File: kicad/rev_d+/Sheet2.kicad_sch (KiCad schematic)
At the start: 199 parts, among them J10 vg_old, J12 JUMPER, J13 RJ45_Hanrun_HR911105A_Horizon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, J5 JUMPER, J6 JUMPER, J8 JUMPER, J9 JUMPER, Q2 QUARTZ, Q3 QUARTZ32768, X11 KEYB-MOUSE, X12 IDC20, X13 USB_C, X15 PLB2-2, X19 WCH LinkE pgm conn, X21 Turbosound conn, X22 PS2 extra input, X23 SEGA pads, X25 USB_C device, X27 USB_A, X3 IDC26LPT, X4 IDC10M, X5 IDC10M, X6 RS232_9

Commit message: pentevo: rev D+: PS/2 WIP
git-svn-id: svn://localhost/local-pentevo@1303 c6c76956-fad2-4150-a3a9-ea0a427205ba
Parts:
- added C65: 10uF, EC-CHIP, symbol eva-altium-import:Sheet1_0_ECAPCHIP
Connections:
- net GND: now also C65.2
- net VCC33_MCU: no longer L6.1
- net VCC3V3: now also R32.1 (i/o), R33.1 (i/o), R34.1 (i/o)
- net VCC5: no longer R32.1 (i/o), R33.1 (i/o), R34.1 (i/o)
- net VCC5_MCU: now also L6.1; no longer X27.1 (VBUS)
- net at C59.1, XSD2.4 (VDD): no longer L6.2
- new net: C65.1, L6.2, X27.1 (VBUS)
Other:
- moved on the sheet: R32, R33, R34, R60, R61, R62, X19

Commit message: pentevo: rev D+: PS/2 WIP
git-svn-id: svn://localhost/local-pentevo@1304 c6c76956-fad2-4150-a3a9-ea0a427205ba
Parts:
- added L7: 1uH, L-CHIP, symbol eva-altium-import:Sheet1_1_L-CHIP
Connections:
- net VCC33_MCU: now also L7.1
- net at C59.1, XSD2.4 (VDD): now also L7.2
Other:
- moved on the sheet: C38, C39, C4, C5, C7, C8, J12, J5, J9, Q2, Q3, R153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

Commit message: pentevo: rev D+: PS/2 WIP
git-svn-id: svn://localhost/local-pentevo@1305 c6c76956-fad2-4150-a3a9-ea0a427205ba
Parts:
- removed R200: 5K1, R-CHIP, symbol eva-altium-import:Sheet2_0_mirrored_RESCHIP
- added R200: 10K, R-CHIP, symbol eva-altium-import:Sheet1_1_RESCHIP
- added R203: 24k, R-CHIP, symbol eva-altium-import:Sheet2_3_RESCHIP
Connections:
- net ATX_POWERON: now also R25.1 (i/o)
- net GND: now also R203.1 (i/o)
- net PS2_KB_CLK_I: now also D4.98 (PE1)
- net PS2_KB_CLK_O: now also D4.24 (PA1)
- net PS2_KB_DAT_I: now also D4.97 (PE0)
- net PS2_KB_DAT_O: now also D4.23 (PA0)
- net PS2_MS_CLK_I: now also D4.2 (PE3)
- net PS2_MS_CLK_O: now also D4.26 (PA3)
- net PS2_MS_DAT_I: now also D4.1 (PE2)
- net PS2_MS_DAT_O: now also D4.25 (PA2)
- net USBDEV_VBUS: now reaches D4.68 (PA9/OTG_VBUS)
- net USBDEV_VBUS: now also R200.2 (i/o1), R203.2 (i/o1)
- net at X25.A4 (VBUS), X25.A9 (VBUS), X25.B4 (VBUS)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: now also R200.1 (i/o)
- no-connect marks 39 -> 38
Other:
- moved on the sheet: R25, R35, VD6

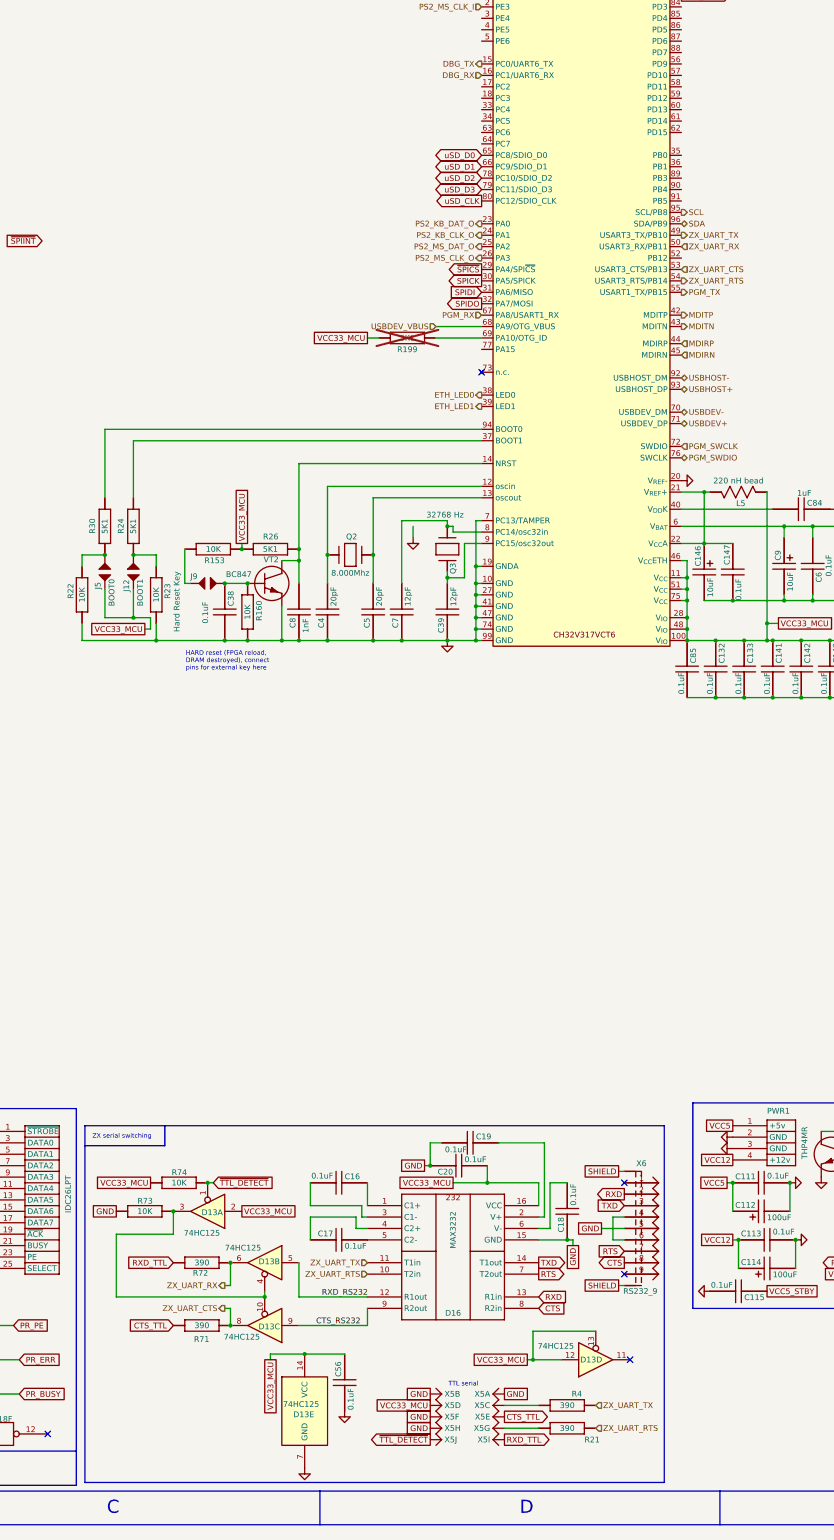
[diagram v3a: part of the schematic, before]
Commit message: pentevo: rev D+: PS/2 done, separate UARTs per TTL and RS232
git-svn-id: svn://localhost/local-pentevo@1306 c6c76956-fad2-4150-a3a9-ea0a427205ba
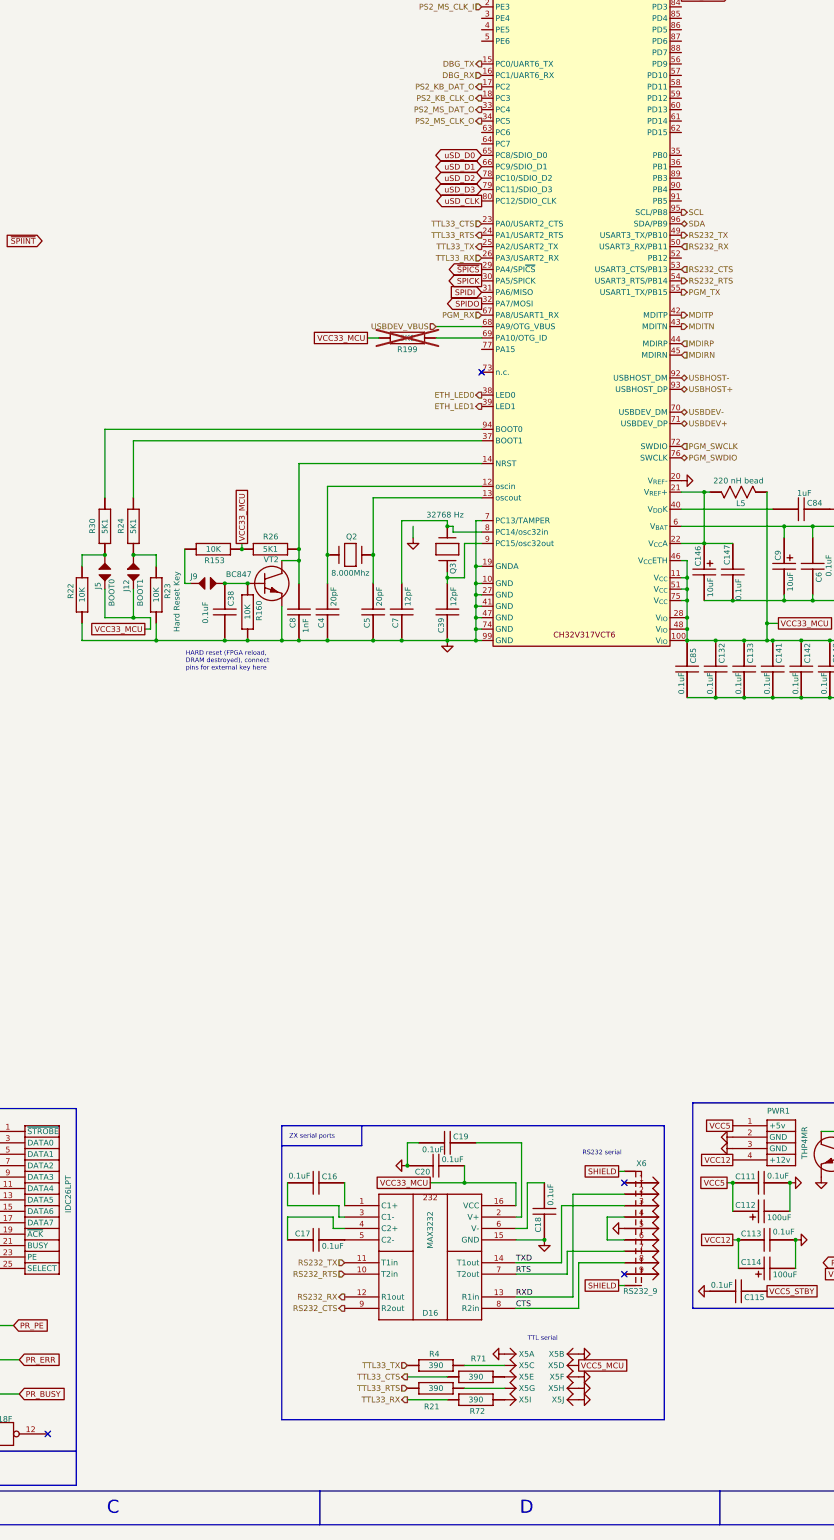
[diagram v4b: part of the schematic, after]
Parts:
- removed C56: 0.1uF, C-CHIP, symbol eva-altium-import:Sheet2_3_mirrored_CAPCHIP
- removed D13: 74HC125, symbol 74xx:74LS125
- removed R73, R74: 10K, R-CHIP, symbol eva-altium-import:Sheet2_2_RESCHIP
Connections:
- net ~{TTL_DETECT} is gone; now on net GND: X5.10
- net PS2_KB_CLK_O: now also D4.18 (PC3); no longer D4.24 (PA1)
- net PS2_KB_DAT_O: now also D4.17 (PC2); no longer D4.23 (PA0)
- net PS2_MS_CLK_O: now also D4.34 (PC5); no longer D4.26 (PA3)
- net PS2_MS_DAT_O: now also D4.33 (PC4); no longer D4.25 (PA2)
- net VCC33_MCU: no longer X5.4
- net VCC5_MCU: now also X5.4
- net CTS_RS232 renamed RS232_CTS
- net RS232_CTS: now also D4.53 (USART3_CTS/PB13)
- net CTS_TTL: no longer names the net of R71.1 (i/o), X5.5
- net RXD_RS232 renamed RS232_RX
- net RS232_RX: now also D4.50 (USART3_RX/PB11)
- net RXD_TTL: no longer names the net of R72.1 (i/o), X5.9
- net ZX_UART_CTS renamed TTL33_CTS
- net TTL33_CTS: now also D4.23 (PA0/USART2_CTS); no longer D4.53 (USART3_CTS/PB13)
- net ZX_UART_RTS renamed RS232_RTS
- net RS232_RTS: no longer R21.2 (i/o1)
- net ZX_UART_RX renamed TTL33_RX
- net TTL33_RX: now also D4.26 (PA3/USART2_RX); no longer D4.50 (USART3_RX/PB11)
- net ZX_UART_TX renamed RS232_TX
- net RS232_TX: no longer R4.1 (i/o)
- new net TTL33_RTS: D4.24 (PA1/USART2_RTS), R21.2 (i/o1)
- new net TTL33_TX: D4.25 (PA2/USART2_TX), R4.1 (i/o)
- no-connect marks 38 -> 37
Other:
- note added: "ZX serial ports"
- note removed: "ZX serial switching"
- moved on the sheet: C16, C17, C18, C19, C20, D16, R21, R4, R71, R72, X5A, X5B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

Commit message: pentevo: rev D+: zx kbd
git-svn-id: svn://localhost/local-pentevo@1307 c6c76956-fad2-4150-a3a9-ea0a427205ba
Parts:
- removed R152, R161: 1K, R-CHIP, symbol eva-altium-import:Sheet2_3_RESCHIP
- removed VT3: BC847, Package_TO_SOT_SMD:SOT-23_Handsoldering, symbol eva-altium-import:Sheet2_0_mirrored_BC847
- added C56: 20pF, C-CHIP, symbol eva-altium-import:Sheet2_0_CAPCHIP
- added J13, J14: JUMPER, JUMPER, symbol eva-altium-import:Sheet2_3_JUMPER
- added R152, R161: 5K1, R-CHIP, symbol eva-altium-import:Sheet2_0_RESCHIP
- added R19, R205: 390, R-CHIP, symbol eva-altium-import:Sheet1_0_RESCHIP
- added R204: 5K1, R-CHIP, symbol eva-altium-import:Sheet2_1_RESCHIP
- added R206: 470K, Resistor_SMD:R_0805_2012Metric_Pad1.20x1.40mm_HandSolder, symbol Device:R
- added R73: 1K, Resistor_SMD:R_0805_2012Metric_Pad1.20x1.40mm_HandSolder, symbol Device:R
- added R74: 390, R-CHIP, symbol eva-altium-import:Sheet2_0_RESCHIP
- added VD3: LED, LED_SMD:LED_0805_2012Metric_Pad1.15x1.40mm_HandSolder, symbol eva-altium-import:Sheet1_0_mirrored_LED
- added VT3, VT4: BC847, Package_TO_SOT_SMD:SOT-23_Handsoldering, symbol Transistor_BJT:BC847
- R36, R37, R38, R39, R40, R41, R42, R43, R44, R45: value 10K -> 5K1
- VD6: footprint LED100 -> LED_SMD:LED_0805_2012Metric_Pad1.15x1.40mm_HandSolder
- renumbered J13 to X28
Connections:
- net ATX_POWERON: now also R73.1, VT3.1 (B)
- net GND: now also R36.1 (i/o), R37.1 (i/o), R38.1 (i/o), R39.1 (i/o), R40.1 (i/o), R73.2, VT3.2 (E), VT4.2 (E)
- net JOYD: now also D4.81 (PD0)
- net JOYF: now also D4.85 (PD4)
- net JOYL: now also D4.82 (PD1)
- net JOYR: now also D4.84 (PD3)
- net JOYU: now also D4.86 (PD5)
- net NMIKEY: now also D4.5 (PE6), R152.2 (i/o1)
- net TAPE_BIT: now also D4.64 (PC7), C56.2, R206.1; no longer D20.8
- net VCC33_MCU: now also R41.1 (i/o), R42.1 (i/o), R43.1 (i/o), R44.1 (i/o), R45.1 (i/o), R152.1 (i/o), R161.1 (i/o); no longer VD6.A
- net VCC5: now also R19.1 (i/o), R205.1 (i/o)
- net VCC5_MCU: now also VD6.A, J13.0 (1); no longer R36.1 (i/o), R37.1 (i/o), R38.1 (i/o), R39.1 (i/o), R40.1 (i/o), R41.1 (i/o), R42.1 (i/o), R43.1 (i/o), R44.1 (i/o), R45.1 (i/o)
- net ZXCOL0: now also D4.35 (PB0)
- net ZXCOL1: now also D4.36 (PB1)
- net ZXCOL2: now also D4.89 (PB3)
- net ZXCOL3: now also D4.90 (PB4)
- net ZXCOL4: now also D4.91 (PB5)
- net ZXROW0: now also D4.88 (PD7)
- net ZXROW1: now also D4.56 (PD9)
- net ZXROW2: now also D4.57 (PD10)
- net ZXROW3: now also D4.58 (PD11)
- net ZXROW4: now also D4.59 (PD12)
- net ZXROW5: now also D4.60 (PD13)
- net ZXROW6: now also D4.61 (PD14)
- net ZXROW7: now also D4.62 (PD15)
- net ~{SOFTRST}: now also D4.4 (PE5), R161.2 (i/o1)
- net ~{SPIINT}: now also D4.3 (PE4)
- net at R25.2 (i/o1): now also D4.77 (PA15)
- net at PWR2.14 (~{PS_ON}): now also VT3.3 (C)
- net ~{PWR_LED}: now reaches R35.1 (i/o)
- net ~{PWR_LED}: now also R74.1 (i/o), VT4.3 (C)
- net at D4.63 (PC6): now also R204.2 (i/o1)
- new net: J13.1 (2), R74.2 (i/o1)
- new net: J14.1 (2), R205.2 (i/o1)
- new net: C56.1, D20.8, R206.2
- new net: R19.2 (i/o1), VD3.A
- new net: R204.1 (i/o), VT4.1 (B)
- new net ~{DISK_LED}: J14.0 (1), VD3.K
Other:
- moved on the sheet: C16, C17, C18, C19, C20, C37, D16, D20D, D20E, D20F, J6, J8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

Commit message: pentevo: rev D+: return back shared UART between TTL and RS232, connect ROM high addrs to MCU
git-svn-id: svn://localhost/local-pentevo@1309 c6c76956-fad2-4150-a3a9-ea0a427205ba
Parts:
- removed C16: 0.1uF, C-CHIP, symbol eva-altium-import:Sheet2_0_mirrored_CAPCHIP
- removed C17: 0.1uF, C-CHIP, symbol eva-altium-import:Sheet2_0_CAPCHIP
- removed C18: 0.1uF, C-CHIP, symbol eva-altium-import:Sheet2_1_CAPCHIP
- removed R21, R4: 390, R-CHIP, symbol eva-altium-import:Sheet2_0_mirrored_RESCHIP
- removed unit 9 of X5
- removed unit 5 of X5
- removed unit 7 of X5
- removed unit 1 of X5
- removed unit 3 of X5
- removed X6: RS232_9, DSUB-9, symbol eva-altium-import:Sheet2_0_mirrored_RS232_9
- added C16: 0.1uF, C-CHIP, symbol eva-altium-import:Sheet2_0_CAPCHIP
- added C17: 0.1uF, C-CHIP, symbol eva-altium-import:Sheet2_3_mirrored_CAPCHIP
- added C18: 0.1uF, C-CHIP, symbol eva-altium-import:Sheet2_0_mirrored_CAPCHIP
- added C82: 0.1uF, C-CHIP, symbol eva-altium-import:Sheet2_1_CAPCHIP
- added D13: 74HC125, symbol 74xx:74LS125
- added R207, R208: 390, R-CHIP, symbol eva-altium-import:Sheet2_0_mirrored_RESCHIP
- added R21, R4: 10K, R-CHIP, symbol eva-altium-import:Sheet2_2_RESCHIP
- added X29: RS232_9, DSUB-9, symbol eva-altium-import:Sheet2_0_mirrored_RS232_9
- added X6: IDC10M, IDC10M, symbol eva-altium-import:Sheet2_2_IDC10M
- R151: value 1K -> 47K
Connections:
- net CTS is gone; now on net RS232_CTS: D16.8 (R2in)
- net RTS is gone; now on net RS232_RTS: D16.7 (T2out)
- net GND: now also C19.1, C20.2, C17.2, C82.1, D13.7 (GND), R4.1 (i/o), X29.5, X6.1; no longer C19.2, C20.1, X5.10
- net PLLS0: now also D4.26 (PA3)
- net PLLS1: now also D4.52 (PB12)
- net PWRGOOD: now also R151.2 (i/o1); no longer R151.1 (i/o)
- net RS232_CTS: now also X29.8; no longer D16.9 (R2out), D4.53 (USART3_CTS/PB13)
- net RS232_RTS: now also X29.7; no longer D16.10 (T2in), D4.54 (USART3_RTS/PB14)
- net SHIELD: now also X29.10, X29.11
- net VCC33_MCU: now also C19.2, C17.1, D13.12, D13.13, D13.14 (VCC), D13.2, R21.2 (i/o1); no longer C20.2
- net at R72.1 (i/o): now also X6.5
- net at D16.2 (V+): now also C20.1; no longer C19.1
- net at R71.1 (i/o): now also X6.9
- net at D30.19 (IO1_6): no longer VT7.3 (D)
- net at D30.18 (IO1_5): no longer VT8.3 (D)
- net at D30.20 (IO1_7): no longer VT6.3 (D)
- net at D16.6 (V-): now also C82.2
- net at D16.1 (C1+): now also C18.1
- net at D16.3 (C1-): now also C18.2
- net at D16.4 (C2+): now also C16.1
- net at D16.5 (C2-): now also C16.2
- net at D4.87 (PD6): now also R151.1 (i/o)
- net RS232_RX: no longer names the net of D16.12 (R1out)
- net RS232_RX: now also D13.5; no longer D4.50 (USART3_RX/PB11)
- net RS232_TX renamed ZX_UART_TX
- net ZX_UART_TX: now also R207.1 (i/o)
- net RXD renamed RS232_RXD
- net RS232_RXD: now also X29.2
- net TTL33_CTS: no longer names the net of D4.23 (PA0)
- net TTL33_CTS: now also VT8.3 (D); no longer R71.2 (i/o1)
- net TTL33_RTS: no longer names the net of D4.24 (PA1)
- net TTL33_RTS: now also VT7.3 (D)
- net TTL33_RX renamed ZX_UART_CTS
- net ZX_UART_CTS: now also D4.53 (USART3_CTS/PB13), D13.8; no longer D4.26 (PA3/USART2_RX)
- net TTL33_TX: no longer names the net of D4.25 (PA2)
- net TTL33_TX: now also VT6.3 (D)
- net TXD renamed RS232_TXD
- net RS232_TXD: now also X29.3
- new net: R207.2 (i/o1), X6.3
- new net: R208.1 (i/o), X6.7
- new net: X29.4, X29.6
- new net: D13.10, D13.3, D13.4, R4.2 (i/o1)
- new net: D13.9, D16.9 (R2out)
- new net ZX_UART_RTS: D16.10 (T2in), D4.54 (USART3_RTS/PB14), R208.2 (i/o1)
- new net ZX_UART_RX: D13.6, D4.50 (USART3_RX/PB11), R71.2 (i/o1)
- new net ~{TTL_DETECT}: D13.1, R21.1 (i/o), X5.10
- no-connect marks 37 -> 38
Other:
- note added: "ZX serial switching"
- note removed: "ZX serial ports"
- moved on the sheet: D17, D18A, D18B, D18C, D18D, D18E, D18F, R14, R29, R57, R68, R69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

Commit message: pentevo: rev D+: fix I2C extender for segapads, remove 2N7002 from high ROM addresses, add I2C level convertor on 2N7002 (because of PCA9555 input levels)
git-svn-id: svn://localhost/local-pentevo@1311 c6c76956-fad2-4150-a3a9-ea0a427205ba
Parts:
- removed VT6, VT7: 2N7002, Package_TO_SOT_SMD:SOT-23, symbol Transistor_FET:2N7002
- added R209: 10K, R-CHIP, symbol eva-altium-import:Sheet2_1_RESCHIP
- added VT9: 2N7002, Package_TO_SOT_SMD:SOT-23, symbol Transistor_FET:2N7002
- D30: Comment (none) -> For segapads
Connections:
- net ROM_STATIC_A19: now also D4.23 (PA0); no longer R186.2 (i/o1), VT8.2 (S)
- net ROM_STATIC_A20: now also D4.24 (PA1); no longer R187.2 (i/o1)
- net ROM_STATIC_A21: now also D4.25 (PA2); no longer R188.2 (i/o1)
- net S2_C/~{START}: now also D30.18 (IO1_5); no longer D30.10 (IO0_6)
- net SCL: now also R209.2 (i/o1), VT9.3 (D); no longer D4.95 (SCL/PB8)
- net SDA: now also R188.2 (i/o1), VT8.3 (D); no longer D4.96 (SDA/PB9)
- net VCC33_MCU: now also R186.2 (i/o1), R187.2 (i/o1), VT8.1 (G), VT9.1 (G)
- net VCC5: now also C122.1, D30.24 (VDD), R209.1 (i/o); no longer R186.1 (i/o), R187.1 (i/o), VT8.1 (G)
- net VCC5_MCU: no longer C122.1, D30.24 (VDD)
- net ZXCOL0: now also R36.2 (i/o1); no longer R40.2 (i/o1)
- net ZXCOL1: now also R37.2 (i/o1); no longer R39.2 (i/o1)
- net ZXCOL3: now also R39.2 (i/o1); no longer R37.2 (i/o1)
- net ZXCOL4: now also R40.2 (i/o1); no longer R36.2 (i/o1)
- net S2_select: now reaches D30.19 (IO1_6)
- net S2_select: now also X23.16 (Pin_16)
- removed net S1+2_select: D30.11 (IO0_7), X23.16 (Pin_16), X23.7 (Pin_7)
- new net S1_select: D30.10 (IO0_6), X23.7 (Pin_7)
- new net SCL_33: D4.95 (SCL/PB8), R187.1 (i/o), VT9.2 (S)
- new net SDA_33: D4.96 (SDA/PB9), R186.1 (i/o), VT8.2 (S)
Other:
- moved on the sheet: C111, C112, C113, C114, C115, C122, D13D, D30, DA7, DA8, J10, PWR1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
